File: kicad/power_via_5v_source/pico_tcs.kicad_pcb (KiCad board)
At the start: 2 copper layers, 65 x 61.5 mm, 11 parts, among them J1 TCS/Power, J2 Conn_01x20_Male, J3 Conn_01x20_Male, J4 Keypad, J5 Display, U2 ULN2003

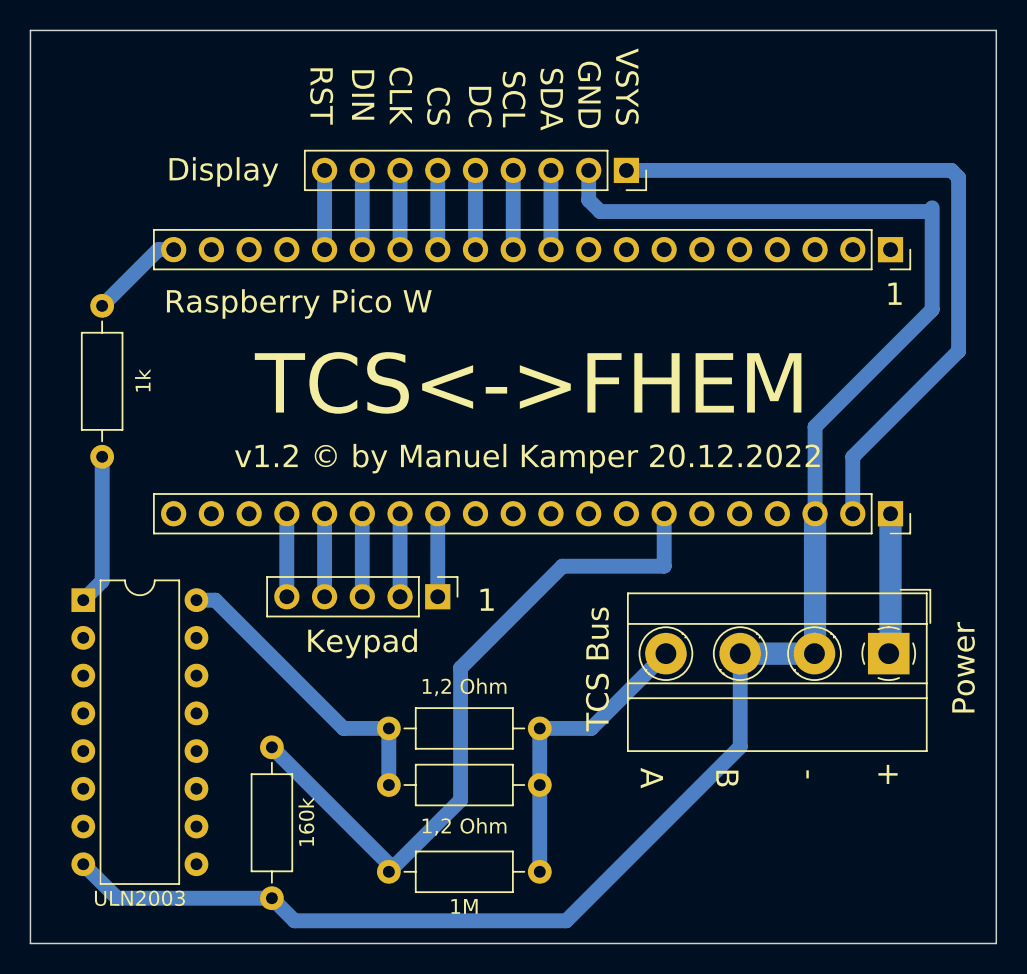
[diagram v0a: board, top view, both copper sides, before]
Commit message: fixed bug in connection between display and pico
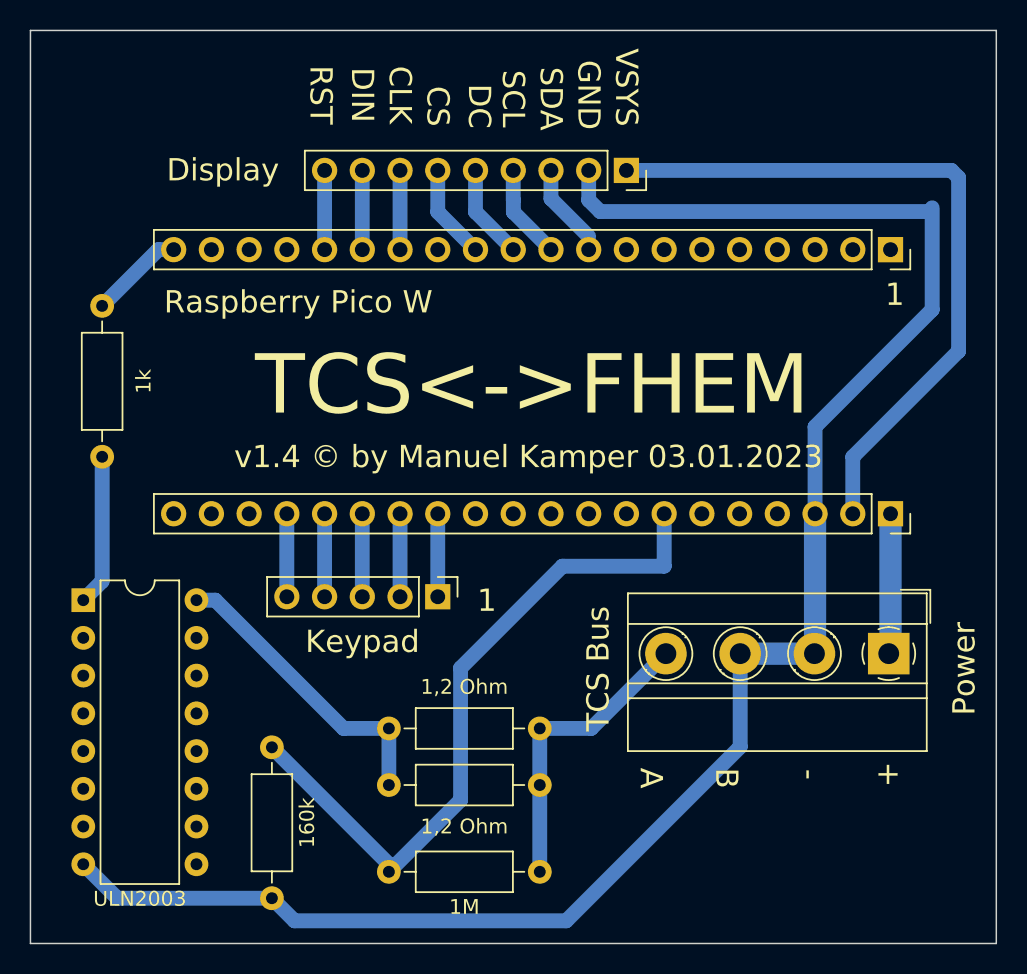
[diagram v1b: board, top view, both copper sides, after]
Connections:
- J2 pad 10: Net-(J2-Pad10) -> Net-(J5-Pad4)
- J2 pad 11: Net-(J2-Pad11) -> Net-(J5-Pad5)
- J2 pad 12: Net-(J2-Pad12) -> Net-(J5-Pad6)
- J2 pad 13: Net-(J2-Pad13) -> unconnected-(J2-Pad13)
- J2 pad 9: unconnected-(J2-Pad9) -> Net-(J2-Pad9)
- J5 pad 3: Net-(J2-Pad10) -> Net-(J2-Pad9)
- J5 pad 4: Net-(J2-Pad11) -> Net-(J5-Pad4)
- J5 pad 5: Net-(J2-Pad12) -> Net-(J5-Pad5)
- J5 pad 6: Net-(J2-Pad13) -> Net-(J5-Pad6)
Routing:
- net Net-(J2-Pad9): track 0.00 -> 6.39 mm
- net Net-(J5-Pad6): track 0.00 -> 6.39 mm
- net Net-(J5-Pad5): track 0.00 -> 6.39 mm
- net Net-(J5-Pad4): track 0.00 -> 6.39 mm
- net Net-(J2-Pad13): track 5.33 -> 0.00 mm
- net Net-(J2-Pad12): track 5.33 -> 0.00 mm
- net Net-(J2-Pad11): track 5.33 -> 0.00 mm
- net Net-(J2-Pad10): track 5.33 -> 0.00 mm
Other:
- board text added: "v1.4 © by Manuel Kamper 03.01.2023"
- board text removed: "v1.2 © by Manuel Kamper 20.12.2022"
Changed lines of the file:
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@@
   (net 7 "unconnected-(J2-Pad7)")
   (net 8 "unconnected-(J2-Pad8)")
-  (net 9 "unconnected-(J2-Pad9)")
+  (net 9 "Net-(J2-Pad9)")
   (net 10 "unconnected-(J2-Pad17)")
   (net 11 "unconnected-(J2-Pad18)")
@@
   (net 27 "Net-(J3-Pad16)")
   (net 28 "Net-(J3-Pad17)")
-  (net 29 "Net-(J2-Pad10)")
-  (net 30 "Net-(J2-Pad11)")
-  (net 31 "Net-(J2-Pad12)")
-  (net 32 "Net-(J2-Pad13)")
+  (net 29 "Net-(J5-Pad4)")
+  (net 30 "Net-(J5-Pad5)")
+  (net 31 "Net-(J5-Pad6)")
+  (net 32 "unconnected-(J2-Pad13)")
   (net 33 "Net-(J2-Pad14)")
   (net 34 "Net-(J2-Pad15)")
@@
       (net 8 "unconnected-(J2-Pad8)") (pinfunction "Pin_8") (pintype "passive"))
     (pad "9" thru_hole oval (at 0 20.32 270) (size 1.7 1.7) (drill 1) (layers *.Cu *.Mask)
-      (net 9 "unconnected-(J2-Pad9)") (pinfunction "Pin_9") (pintype "passive"))
+      (net 9 "Net-(J2-Pad9)") (pinfunction "Pin_9") (pintype "passive"))
     (pad "10" thru_hole oval (at 0 22.86 270) (size 1.7 1.7) (drill 1) (layers *.Cu *.Mask)
-      (net 29 "Net-(J2-Pad10)") (pinfunction "Pin_10") (pintype "passive"))
+      (net 29 "Net-(J5-Pad4)") (pinfunction "Pin_10") (pintype "passive"))
     (pad "11" thru_hole oval (at 0 25.4 270) (size 1.7 1.7) (drill 1) (layers *.Cu *.Mask)
-      (net 30 "Net-(J2-Pad11)") (pinfunction "Pin_11") (pintype "passive"))
+      (net 30 "Net-(J5-Pad5)") (pinfunction "Pin_11") (pintype "passive"))
     (pad "12" thru_hole oval (at 0 27.94 270) (size 1.7 1.7) (drill 1) (layers *.Cu *.Mask)
-      (net 31 "Net-(J2-Pad12)") (pinfunction "Pin_12") (pintype "passive"))
+      (net 31 "Net-(J5-Pad6)") (pinfunction "Pin_12") (pintype "passive"))
     (pad "13" thru_hole oval (at 0 30.48 270) (size 1.7 1.7) (drill 1) (layers *.Cu *.Mask)
-      (net 32 "Net-(J2-Pad13)") (pinfunction "Pin_13") (pintype "passive"))
+      (net 32 "unconnected-(J2-Pad13)") (pinfunction "Pin_13") (pintype "passive"))
     (pad "14" thru_hole oval (at 0 33.02 270) (size 1.7 1.7) (drill 1) (layers *.Cu *.Mask)
       (net 33 "Net-(J2-Pad14)") (pinfunction "Pin_14") (pintype "passive"))
@@
       (net 2 "GND") (pinfunction "Pin_2") (pintype "passive"))
     (pad "3" thru_hole oval (at 0 5.08 270) (size 1.7 1.7) (drill 1) (layers *.Cu *.Mask)
-      (net 29 "Net-(J2-Pad10)") (pinfunction "Pin_3") (pintype "passive"))
+      (net 9 "Net-(J2-Pad9)") (pinfunction "Pin_3") (pintype "passive"))
     (pad "4" thru_hole oval (at 0 7.62 270) (size 1.7 1.7) (drill 1) (layers *.Cu *.Mask)
-      (net 30 "Net-(J2-Pad11)") (pinfunction "Pin_4") (pintype "passive"))
+      (net 29 "Net-(J5-Pad4)") (pinfunction "Pin_4") (pintype "passive"))
     (pad "5" thru_hole oval (at 0 10.16 270) (size 1.7 1.7) (drill 1) (layers *.Cu *.Mask)
-      (net 31 "Net-(J2-Pad12)") (pinfunction "Pin_5") (pintype "passive"))
+      (net 30 "Net-(J5-Pad5)") (pinfunction "Pin_5") (pintype "passive"))
     (pad "6" thru_hole oval (at 0 12.7 270) (size 1.7 1.7) (drill 1) (layers *.Cu *.Mask)
-      (net 32 "Net-(J2-Pad13)") (pinfunction "Pin_6") (pintype "passive"))
+      (net 31 "Net-(J5-Pad6)") (pinfunction "Pin_6") (pintype "passive"))
     (pad "7" thru_hole oval (at 0 15.24 270) (size 1.7 1.7) (drill 1) (layers *.Cu *.Mask)
       (net 33 "Net-(J2-Pad14)") (pinfunction "Pin_7") (pintype "passive"))
@@
     (effects (font (size 1.5 1.5) (thickness 0.3)))
   )
-  (gr_text "v1.2 © by Manuel Kamper 20.12.2022" (at 181.864 99.822) (layer "F.SilkS")
+  (gr_text "v1.4 © by Manuel Kamper 03.01.2023" (at 181.864 99.822) (layer "F.SilkS")
     (effects (font (size 1.5 1.5) (thickness 0.375)))
   )
@@
   (segment (start 208.788 83.312) (end 209.042 83.058) (width 0.25) (layer "B.Cu") (net 2))
   (segment (start 201.118 113.075) (end 196.118 113.075) (width 1.5) (layer "B.Cu") (net 2))
+  (segment (start 183.378 80.543) (end 183.378 82.446604) (width 1) (layer "B.Cu") (net 9))
+  (segment (start 183.378 82.446604) (end 185.918 84.986604) (width 1) (layer "B.Cu") (net 9))
+  (segment (start 185.918 84.986604) (end 185.918 85.877) (width 0.25) (layer "B.Cu") (net 9))
   (segment (start 175.758 103.657) (end 175.758 109.245) (width 1) (layer "B.Cu") (net 24))
   (segment (start 173.218 103.657) (end 173.218 109.245) (width 1) (layer "B.Cu") (net 25))
@@
   (segment (start 168.138 103.657) (end 168.138 109.245) (width 1) (layer "B.Cu") (net 27))
   (segment (start 165.598 103.657) (end 165.598 109.245) (width 1) (layer "B.Cu") (net 28))
-  (segment (start 183.378 80.543) (end 183.378 85.877) (width 1) (layer "B.Cu") (net 29))
-  (segment (start 180.838 80.543) (end 180.838 85.877) (width 1) (layer "B.Cu") (net 30))
-  (segment (start 178.298 80.543) (end 178.298 85.877) (width 1) (layer "B.Cu") (net 31))
-  (segment (start 175.758 80.543) (end 175.758 85.877) (width 1) (layer "B.Cu") (net 32))
+  (segment (start 180.848 83.347) (end 180.848 82.55) (width 1) (layer "B.Cu") (net 29))
+  (segment (start 180.848 82.55) (end 180.838 82.54) (width 0.25) (layer "B.Cu") (net 29))
+  (segment (start 183.378 85.877) (end 180.848 83.347) (width 1) (layer "B.Cu") (net 29))
+  (segment (start 180.838 82.54) (end 180.838 80.543) (width 1) (layer "B.Cu") (net 29))
+  (segment (start 178.298 83.337) (end 178.298 80.543) (width 1) (layer "B.Cu") (net 30))
+  (segment (start 180.838 85.877) (end 178.298 83.337) (width 1) (layer "B.Cu") (net 30))
+  (segment (start 178.298 85.877) (end 175.758 83.337) (width 1) (layer "B.Cu") (net 31))
+  (segment (start 175.758 83.337) (end 175.758 80.543) (width 1) (layer "B.Cu") (net 31))
   (segment (start 173.218 80.543) (end 173.218 85.877) (width 1) (layer "B.Cu") (net 33))
   (segment (start 170.678 80.543) (end 170.678 85.877) (width 1) (layer "B.Cu") (net 34))
